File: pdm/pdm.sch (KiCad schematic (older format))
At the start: 31 parts, among them J1 Conn_01x04_Male, J2 Conn_01x06_Female, J3 Conn_01x04_Female, J4 Conn_01x12_Male, M1 Fan, M2 Fan, SW1 SW_Push, U1 SN65HVD233, U2 STM32F042G6Ux, Y1 Crystal_GND24

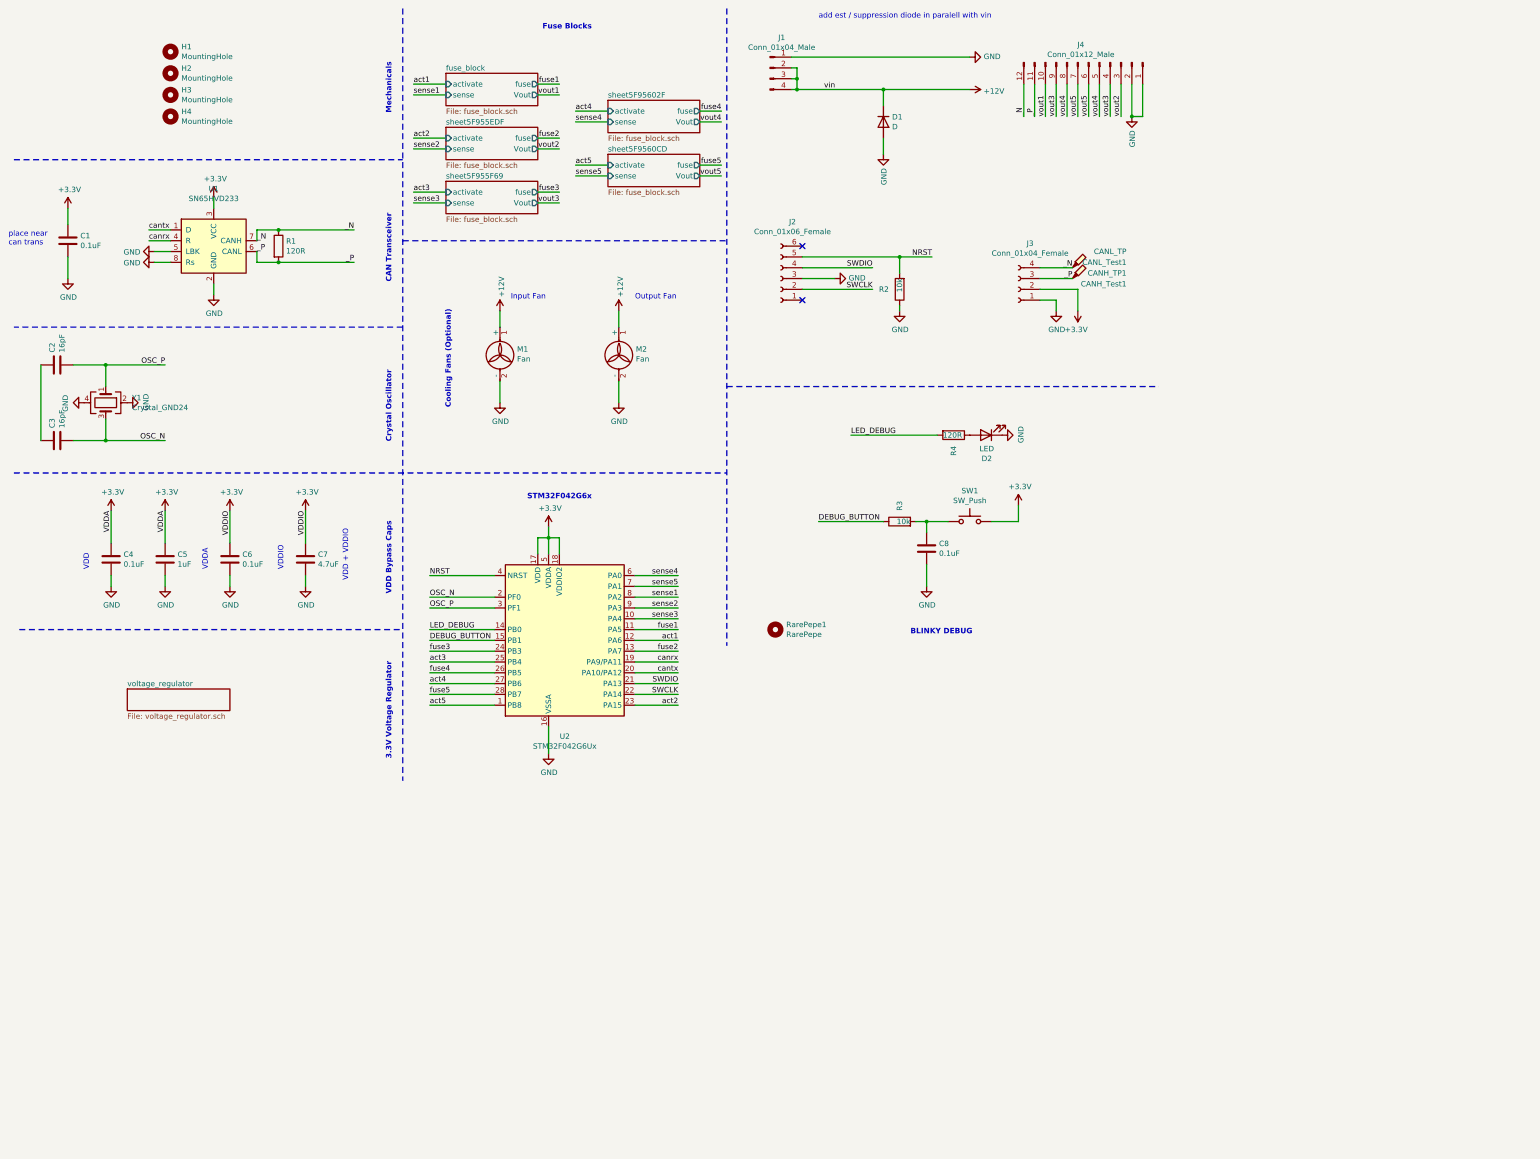
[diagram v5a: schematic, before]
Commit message: major redesign - hc switching output
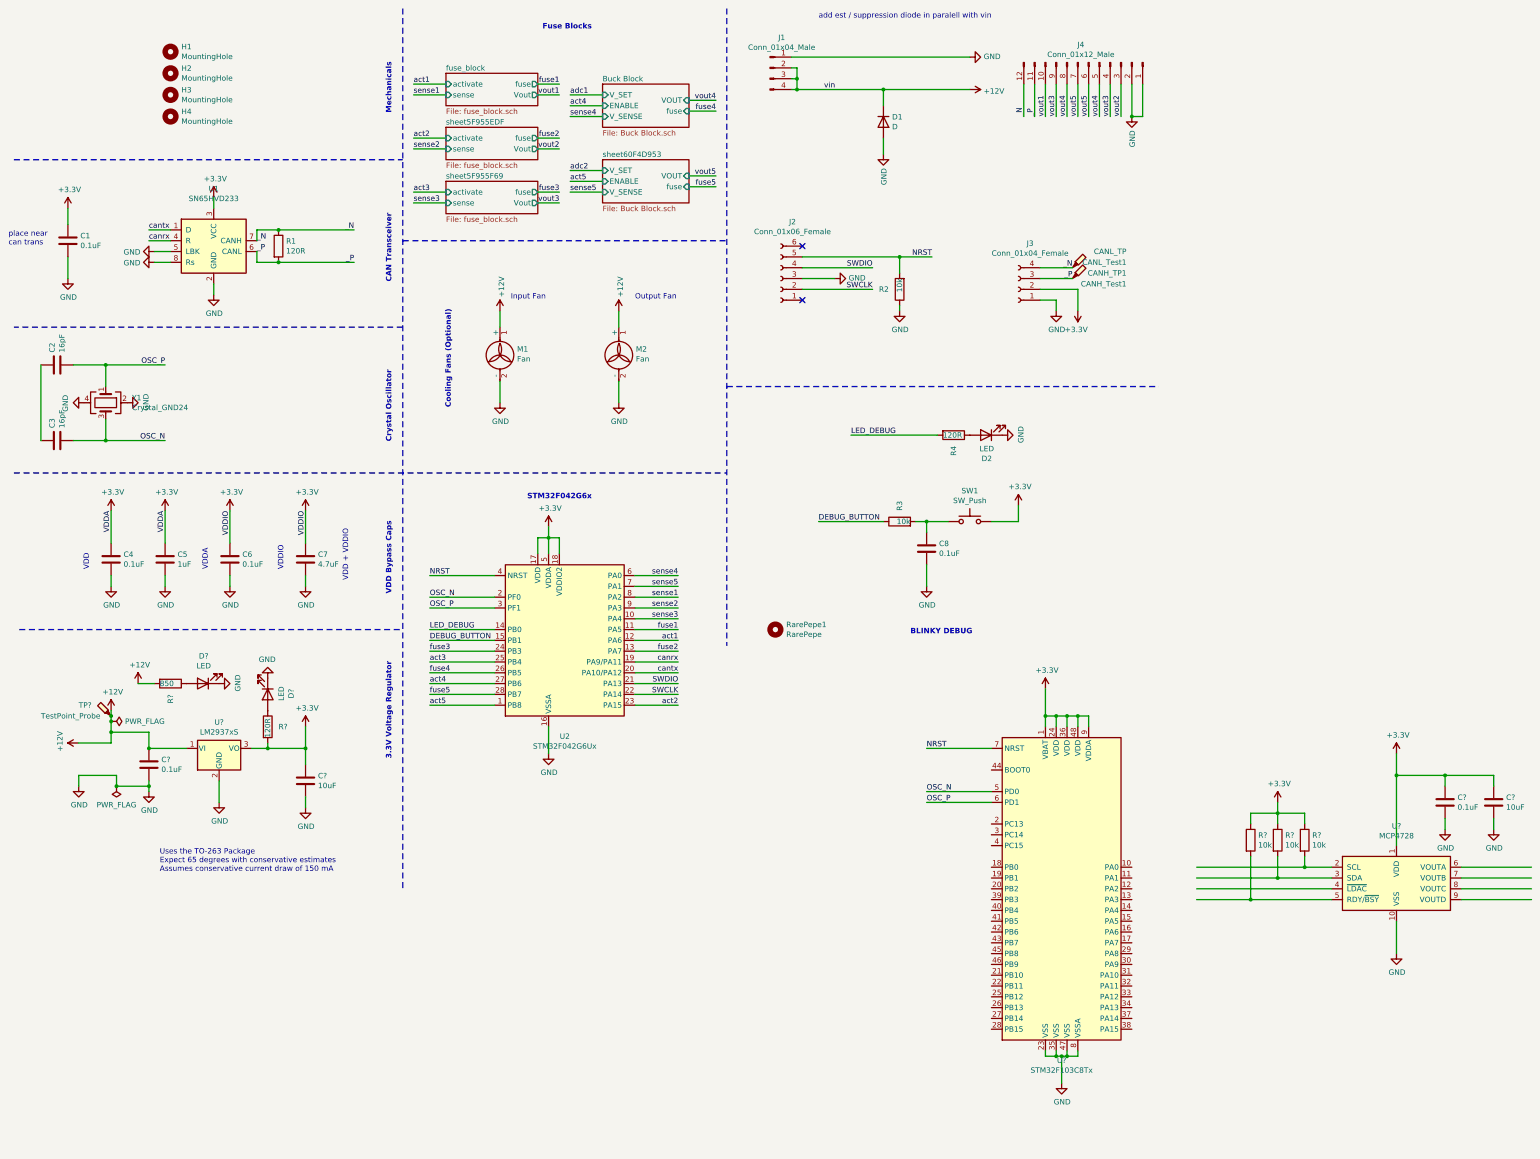
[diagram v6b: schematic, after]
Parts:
- added C? (x2): 10uF, symbol Device:C
- added C?: 0.1uF, symbol Device:C
- added C?: 0.1uF, Capacitor_SMD:C_0805_2012Metric_Pad1.18x1.45mm_HandSolder, symbol Device:C
- added D? (x2): LED, LED_SMD:LED_0805_2012Metric_Pad1.15x1.40mm_HandSolder, symbol pdm-rescue:LED-Device
- added R? (x3): 10k, symbol Device:R
- added R?: 850, Resistor_SMD:R_0805_2012Metric_Pad1.20x1.40mm_HandSolder, symbol pdm-rescue:R-Device
- added R?: 120R, Resistor_SMD:R_0805_2012Metric_Pad1.20x1.40mm_HandSolder, symbol pdm-rescue:R-Device
- added TP?: TestPoint_Probe, TestPoint:TestPoint_Pad_D1.0mm, symbol pdm-rescue:TestPoint_Probe-Connector
- added U?: STM32F103C8Tx, Package_QFP:LQFP-48_7x7mm_P0.5mm, symbol MCU_ST_STM32F1:STM32F103C8Tx
- added U?: MCP4728, Package_SO:MSOP-10_3x3mm_P0.5mm, symbol Analog_DAC:MCP4728
- added U?: LM2937xS, Package_TO_SOT_SMD:TO-263-3_TabPin2, symbol Regulator_Linear:LM2937xS
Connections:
- net labels added: adc1, adc2
- wire segments 128 -> 203
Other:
- note added: "Uses the TO-263 Package\nExpect 65 degrees with conservative estimates\nAssumes conservative current draw of 150 mA"

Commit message: fixed schematic
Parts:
- removed C8: 0.1uF, Capacitor_SMD:C_0805_2012Metric_Pad1.18x1.45mm_HandSolder, symbol pdm-rescue:C-Device
- removed C?: 10uF, symbol Device:C
- removed C?: 0.1uF, symbol Device:C
- removed D2, D?: LED, LED_SMD:LED_0805_2012Metric_Pad1.15x1.40mm_HandSolder, symbol pdm-rescue:LED-Device
- removed J2: Conn_01x06_Female, Connector_PinSocket_2.54mm:PinSocket_1x06_P2.54mm_Vertical_SMD_Pin1Left, symbol Connector:Conn_01x06_Female
- removed R2, R3: 10k, Resistor_SMD:R_0805_2012Metric_Pad1.20x1.40mm_HandSolder, symbol pdm-rescue:R-Device
- removed R4: 120R, Resistor_SMD:R_0805_2012Metric_Pad1.20x1.40mm_HandSolder, symbol pdm-rescue:R-Device
- removed R? (x3): 10k, symbol Device:R
- removed R?: 850, Resistor_SMD:R_0805_2012Metric_Pad1.20x1.40mm_HandSolder, symbol pdm-rescue:R-Device
- removed SW1: SW_Push, Button_Switch_THT:SW_PUSH_6mm, symbol pdm-rescue:SW_Push-Switch
- removed U2: STM32F042G6Ux, Package_DFN_QFN:QFN-28_4x4mm_P0.5mm, symbol pdm-rescue:STM32F042G6Ux-MCU_ST_STM32F0
- removed U?: STM32F103C8Tx, Package_QFP:LQFP-48_7x7mm_P0.5mm, symbol MCU_ST_STM32F1:STM32F103C8Tx
- removed U?: MCP4728, Package_SO:MSOP-10_3x3mm_P0.5mm, symbol Analog_DAC:MCP4728
- removed Y1: Crystal_GND24, Crystal:Crystal_SMD_3225-4Pin_3.2x2.5mm_HandSoldering, symbol Device:Crystal_GND24
- added C10: C, Capacitor_SMD:C_0603_1608Metric, symbol Device:C
- added J2: Conn_01x04_Female, Connector_PinHeader_2.54mm:PinHeader_1x04_P2.54mm_Vertical, symbol Connector:Conn_01x04_Female
- added U3: STM32L496RGTx, Package_QFP:LQFP-64_10x10mm_P0.5mm, symbol MCU_ST_STM32L4:STM32L496RGTx
- added Y1: 32Mhz, Crystal:Crystal_SMD_HC49-SD, symbol Device:Crystal
- C1, C2, C3, C4, C5: footprint Capacitor_SMD:C_0805_2012Metric_Pad1.18x1.45mm_HandSolder -> Capacitor_SMD:C_0603_1608Metric
- C6: renamed from C?; footprint Capacitor_SMD:C_0805_2012Metric_Pad1.18x1.45mm_HandSolder -> Capacitor_SMD:C_0603_1608Metric
- C7: renamed from C6; footprint Capacitor_SMD:C_0805_2012Metric_Pad1.18x1.45mm_HandSolder -> Capacitor_SMD:C_0603_1608Metric
- C8: renamed from C7; footprint Capacitor_SMD:C_0805_2012Metric_Pad1.18x1.45mm_HandSolder -> Capacitor_SMD:C_0603_1608Metric
- C9: renamed from C?; footprint (none) -> Capacitor_SMD:C_0603_1608Metric
- gave numbers to parts that had none: 4
- renumbered D1 to D2
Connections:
- net labels added: DAC1, DAC2
- net labels removed: DEBUG_BUTTON, LED_DEBUG, adc1, adc2
- wire segments 203 -> 159
- no-connect marks 2 -> 29
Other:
- note added: "MISC"
- note removed: "BLINKY DEBUG"
- note removed: "Cooling Fans (Optional)"
- note removed: "Mechanicals"
- note removed: "STM32F042G6x"
- moved on the sheet: C1, C2, C3, C4, C5, C6, C7, C8, C9, CANH_TP1, CANL_Test1, D1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

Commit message: new layout
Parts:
- removed J3: Conn_01x04_Female, Connector_PinSocket_2.54mm:PinSocket_1x04_P2.54mm_Vertical_SMD_Pin1Left, symbol Connector:Conn_01x04_Female
- removed M1, M2: Fan, Connector_JST:JST_EH_B2B-EH-A_1x02_P2.50mm_Vertical, symbol Motor:Fan
- removed RarePepe1: RarePepe, pdm_v2:rarepepe, symbol Mechanical:MountingHole
- C10: value C -> 1uF
- D1: footprint LED_SMD:LED_0805_2012Metric_Pad1.15x1.40mm_HandSolder -> LED_SMD:LED_0603_1608Metric
- R1: footprint Capacitor_SMD:C_0805_2012Metric_Pad1.18x1.45mm_HandSolder -> Resistor_SMD:R_0603_1608Metric
- R2: footprint Resistor_SMD:R_0805_2012Metric_Pad1.20x1.40mm_HandSolder -> Resistor_SMD:R_0603_1608Metric
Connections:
- net GND: now also C2.1, C3.1
- net sense1: no longer U3.9 (PC1)
- net sense2: no longer U3.8 (PC0)
- net sense4: no longer U3.11 (PC3)
- net sense5: no longer U3.10 (PC2)
- no-connect marks 29 -> 24
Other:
- note removed: "Input Fan"
- note removed: "Output Fan"
- moved on the sheet: CANH_TP1, CANL_Test1, TP1
